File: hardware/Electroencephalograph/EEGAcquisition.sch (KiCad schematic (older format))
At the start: 9 parts, among them U1 ADS1298IPAG, U2 OPA330xxD

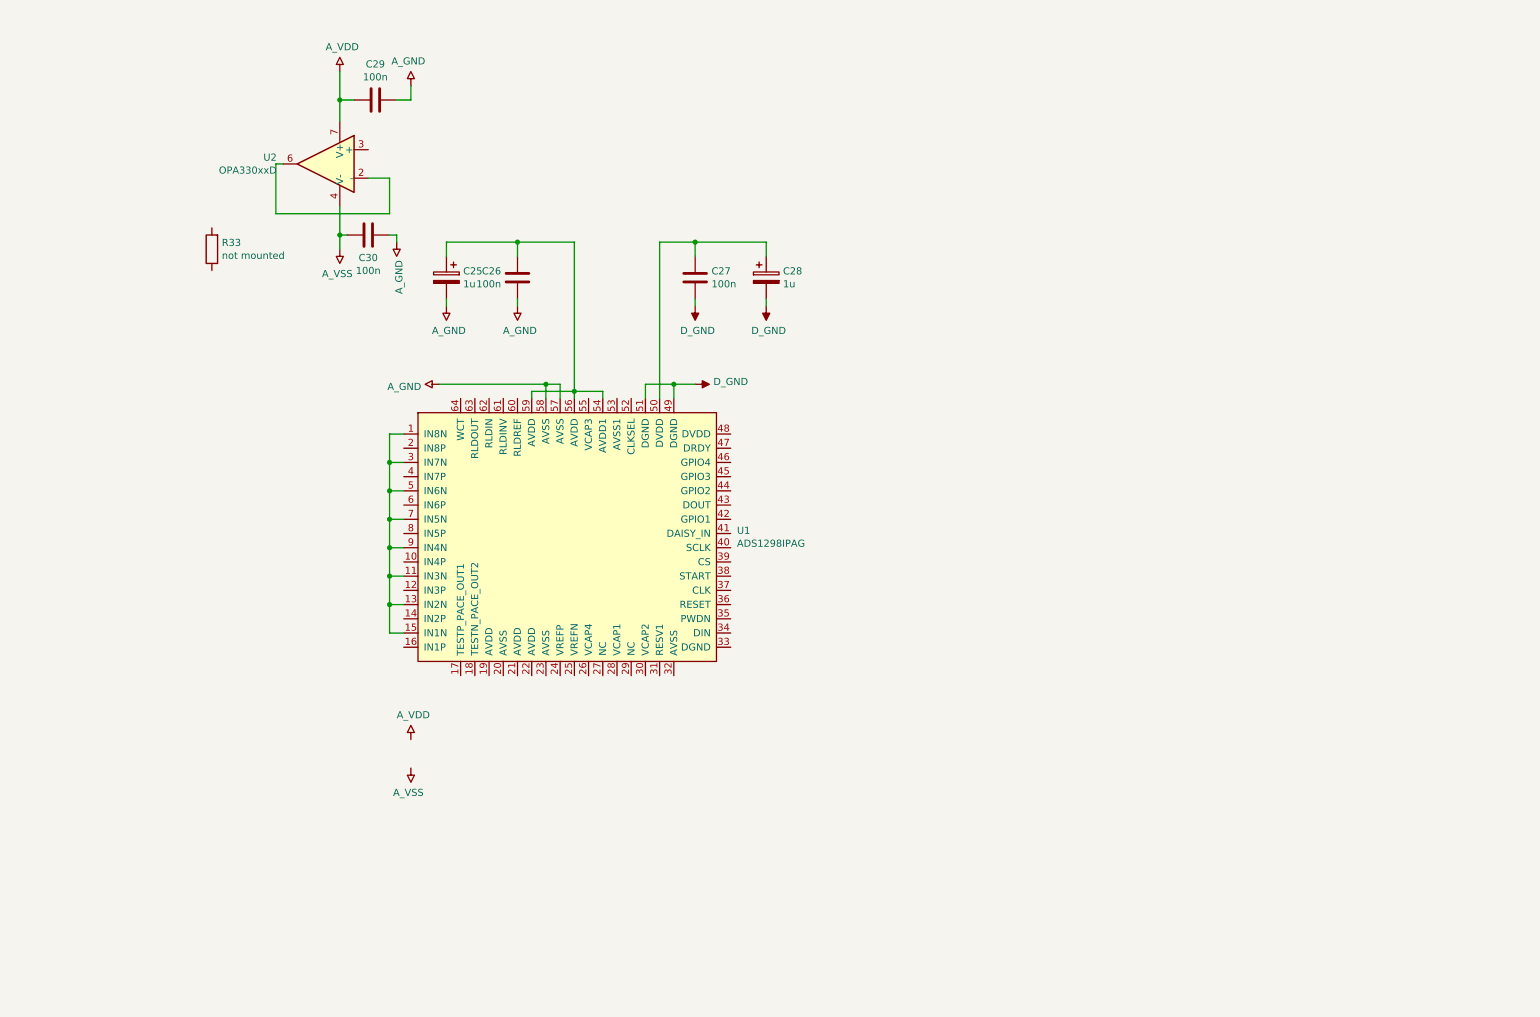
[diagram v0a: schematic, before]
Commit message: paritial routing for analog part
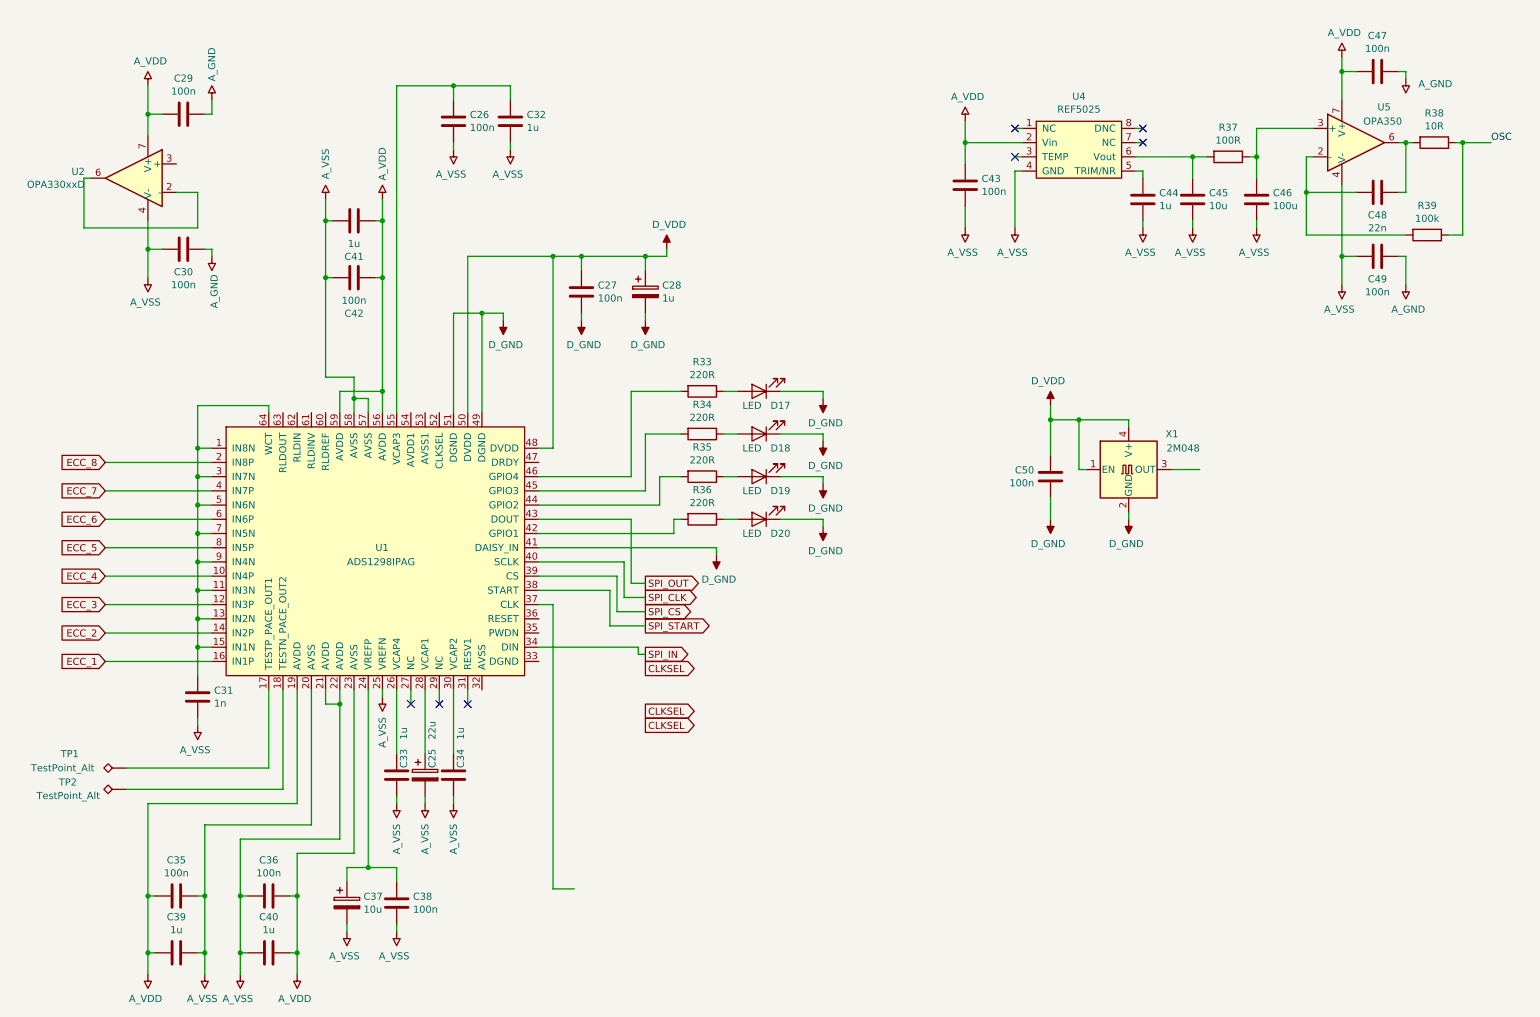
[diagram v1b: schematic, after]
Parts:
- added C31: 1n, Capacitor_SMD:C_0402_1005Metric, symbol Device:C
- added C32, C33, C34, C39, C40, C41, C44: 1u, Capacitor_SMD:C_0402_1005Metric, symbol Device:C
- added C35, C36, C38, C42, C43, C47, C49, C50: 100n, Capacitor_SMD:C_0402_1005Metric, symbol Device:C
- added C37: 10u, Capacitor_Tantalum_SMD:CP_EIA-3528-21_Kemet-B, symbol Device:CP
- added C45: 10u, Capacitor_SMD:C_0402_1005Metric, symbol Device:C
- added C46: 100u, Capacitor_SMD:C_0402_1005Metric, symbol Device:C
- added C48: 22n, Capacitor_SMD:C_0402_1005Metric, symbol Device:C
- added D17, D18, D19, D20: LED, LED_SMD:LED_0603_1608Metric, symbol Device:LED
- added R34, R35, R36: 220R, Resistor_SMD:R_0402_1005Metric, symbol Device:R
- added R37: 100R, Resistor_SMD:R_0402_1005Metric, symbol Device:R
- added R38: 10R, Resistor_SMD:R_0402_1005Metric, symbol Device:R
- added R39: 100k, Resistor_SMD:R_0402_1005Metric, symbol Device:R
- added TP1, TP2: TestPoint_Alt, TestPoint:TestPoint_Pad_2.5x2.5mm, symbol Connector:TestPoint_Alt
- added U4: REF5025, Package_SO:VSSOP-8_2.3x2mm_P0.5mm, symbol Electroencephalograph:REF5025
- added U5: OPA350, Package_SO:SOIC-8_3.9x4.9mm_P1.27mm, symbol Electroencephalograph:OPA350
- added X1: 2M048, Oscillator:Oscillator_SMD_EuroQuartz_XO53-4Pin_5.0x3.2mm, symbol Oscillator:XO91
- C25: value 1u -> 22u
- R33: value not mounted -> 220R
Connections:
- net GNDA: now also U1.41 (DAISY_IN), C47.1, C49.1, C50.2, D17.1 (K), D18.1 (K), D19.1 (K), D20.1 (K), X1.2 (GND); no longer C25.2, C26.2, U1.57 (AVSS), U1.58 (AVSS)
- net VDDA: now also C25.2, C26.2, C27.1, C28.1, U1.19 (AVDD), U1.20 (AVSS), U1.21 (AVDD), U1.22 (AVDD), U1.23 (AVSS), U1.25 (VREFN~), U1.48 (DVDD), U1.50 (DVDD), U1.56 (AVDD), U1.57 (AVSS), U1.58 (AVSS), U1.59 (AVDD), C31.2, C32.2, C33.2, C34.2, C35.1, C35.2, C36.1, C36.2, C37.2, C38.2, C39.1, C39.2, C40.1, C40.2, C41.1, C41.2, C42.1, C42.2, C43.1, C43.2, C44.2, C45.2, C46.2, C47.2, C49.2, C50.1, U4.2 (Vin), U4.4 (GND), U5.4 (V-), U5.7 (V+), X1.1 (EN), X1.4 (V+)
- net at U1.1 (IN8N), U1.11 (IN3N), U1.13 (IN2N)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: now also U1.64 (WCT), C31.1
- net ECC_4: now reaches U1.10 (IN4P)
- net ECC_3: now reaches U1.12 (IN3P)
- net ECC_2: now reaches U1.14 (IN2P~)
- net ECC_1: now reaches U1.16 (IN1P)
- net at U1.17 (TESTP_PACE_OUT1): now also TP1.1
- net at U1.18 (TESTN_PACE_OUT2): now also TP2.1
- net ECC_8: now reaches U1.2 (IN8P)
- net at U1.24 (VREFP): now also C37.1, C38.1
- net at U1.26 (VCAP4): now also C33.1
- net at U1.28 (VCAP1): now also C25.1
- net at U1.30 (VCAP2): now also C34.1
- net SPI_IN: now reaches U1.34 (DIN)
- net SPI_START: now reaches U1.38 (START)
- net SPI_CS: now reaches U1.39 (CS)
- net ECC_7: now reaches U1.4 (IN7P)
- net SPI_CLK: now reaches U1.40 (SCLK)
- net at U1.42 (GPIO1): now also R36.2
- net SPI_OUT: now reaches U1.43 (DOUT)
- net at U1.44 (GPIO2): now also R35.2
- net at U1.45 (GPIO3): now also R34.2
- net at U1.46 (GPIO4): now also R33.2
- net at U1.55 (VCAP3): now also C26.1, C32.1
- net ECC_6: now reaches U1.6 (IN6P)
- net ECC_5: now reaches U1.8 (IN5P)
- net at R33.1: now also D17.2 (A)
- new net: D20.2 (A), R36.1
- new net: D19.2 (A), R35.1
- new net: D18.2 (A), R34.1
- new net: C44.1, U4.5 (TRIM/NR)
- new net: C45.1, R37.2, U4.6 (Vout)
- new net: C46.1, R37.1, U5.3 (+)
- new net: C48.2, R39.2, U5.2 (-)
- new net: C48.1, R38.2, U5.6
- new net OSC: R38.1, R39.1
- now unconnected: U1.54 (AVDD1)
- no-connect marks 0 -> 7
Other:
- moved on the sheet: C25, C26, C27, C28, C29, C30, U1, U2

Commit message: added spi isolator circuit
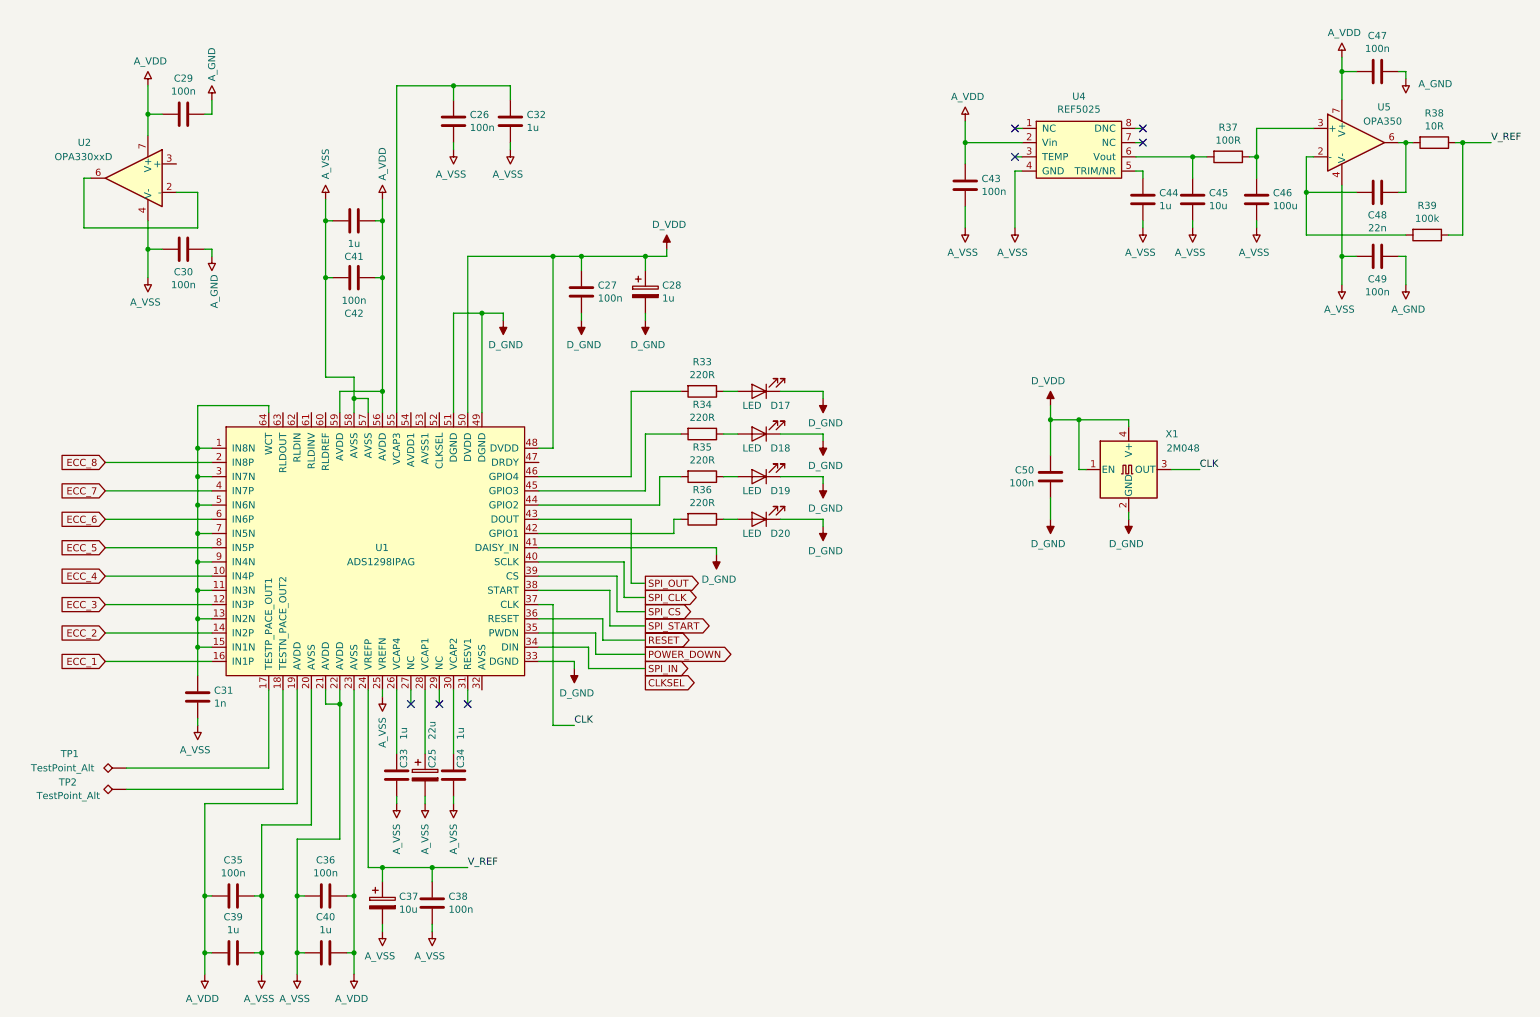
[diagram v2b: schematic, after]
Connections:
- net OSC is gone; now on net V_REF: R38.1, R39.1
- net GNDA: now also U1.33 (DGND)
- net V_REF: now reaches C37.1, C38.1, U1.24 (VREFP)
- net POWER_DOWN: now reaches U1.35 (PWDN)
- net RESET: now reaches U1.36 (RESET)
- net CLK: now reaches U1.37 (CLK)
- net CLK: now also X1.3 (OUT)
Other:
- moved on the sheet: C35, C36, C37, C38, C39, C40
